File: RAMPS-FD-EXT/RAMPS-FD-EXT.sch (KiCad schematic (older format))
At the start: 23 parts, among them J101 NET-TIE, M101 LOGO_OSHW, M102 PCB_GREEN_RMC, P101 CONN_2, P102 CONN_2, P103 CONN_10, U101 LM7809, U102 74HC595, U103 74HC595

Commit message: EXT4: update schematic, layout
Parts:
- removed P103: CONN_10, symbol CONN_10
- added P103: CONN_4, symbol CONN_4
- added P104: CONN_4X2, symbol CONN_4X2
- gave numbers to parts that had none: 1
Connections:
- net labels added: +5V
- wire segments 75 -> 79
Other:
- moved on the sheet: C101, C104, F101, F102, H101, H102, H103, H104, J101, J102, M101, M102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

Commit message: RAMPS-FD-EXT: update, schematic, routing and gerbers
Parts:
- added JP101: VLOG_SEL, ~, symbol JUMP_MINI_3
- P101: value CONN_2 -> MOTOR
- P102: value CONN_2 -> HEATER
- P103: value CONN_4 -> I2C
- P104: value CONN_4X2 -> SPI
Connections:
- net +5V: now also JP101.3
- net +V_LOGIC: now also JP101.2; no longer P103.1 (P1)
- new net VREF: JP101.1, P103.1 (P1)
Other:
- note added: "Select logic voltage"
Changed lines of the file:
@@
 Sheet 1 4
 Title ""
-Date "26 sep 2013"
+Date "6 oct 2013"
 Rev ""
 Comp ""
@@
 L VCC #PWR02
 U 1 1 523CE64B
-P 1850 2400
-F 0 "#PWR02" H 1850 2500 30  0001 C CNN
-F 1 "VCC" H 1850 2500 30  0000 C CNN
-F 2 "" H 1850 2400 60  0001 C CNN
-F 3 "" H 1850 2400 60  0001 C CNN
-	1    1850 2400
+P 3400 3650
+F 0 "#PWR02" H 3400 3750 30  0001 C CNN
+F 1 "VCC" H 3400 3750 30  0000 C CNN
+F 2 "" H 3400 3650 60  0001 C CNN
+F 3 "" H 3400 3650 60  0001 C CNN
+	1    3400 3650
 	1    0    0    -1
 $EndComp
@@
 $Comp
 L PWR_FLAG #FLG014
-U 1 1 523B8CDB
-P 2200 2450
-F 0 "#FLG014" H 2200 2545 30  0001 C CNN
-F 1 "PWR_FLAG" H 2200 2630 30  0000 C CNN
-F 2 "" H 2200 2450 60  0001 C CNN
-F 3 "" H 2200 2450 60  0001 C CNN
-	1    2200 2450
-	1    0    0    -1
-$EndComp
-$Comp
-L PWR_FLAG #FLG015
 U 1 1 523B8CDA
 P 3150 5350
-F 0 "#FLG015" H 3150 5445 30  0001 C CNN
+F 0 "#FLG014" H 3150 5445 30  0001 C CNN
 F 1 "PWR_FLAG" H 3150 5530 30  0000 C CNN
 F 2 "" H 3150 5350 60  0001 C CNN
@@
 $EndComp
 $Comp
-L PWR_FLAG #FLG016
+L PWR_FLAG #FLG015
 U 1 1 523B8CD9
 P 2700 4400
-F 0 "#FLG016" H 2700 4495 30  0001 C CNN
+F 0 "#FLG015" H 2700 4495 30  0001 C CNN
 F 1 "PWR_FLAG" H 2700 4580 30  0000 C CNN
 F 2 "" H 2700 4400 60  0001 C CNN
@@
 $EndSheet
 $Comp
-L GNDPWR #PWR017
+L GNDPWR #PWR016
 U 1 1 523B79D2
 P 2700 5700
-F 0 "#PWR017" H 2700 5750 40  0001 C CNN
+F 0 "#PWR016" H 2700 5750 40  0001 C CNN
 F 1 "GNDPWR" H 2700 5620 40  0000 C CNN
 F 2 "" H 2700 5700 60  0001 C CNN
@@
 $EndComp
 $Comp
-L GNDPWR #PWR018
+L GNDPWR #PWR017
 U 1 1 523B79C1
 P 2400 4650
-F 0 "#PWR018" H 2400 4700 40  0001 C CNN
+F 0 "#PWR017" H 2400 4700 40  0001 C CNN
 F 1 "GNDPWR" H 2400 4570 40  0000 C CNN
 F 2 "" H 2400 4650 60  0001 C CNN
@@
 $EndComp
 $Comp
-L GND #PWR019
+L GND #PWR018
 U 1 1 523B79A8
 P 1450 1600
-F 0 "#PWR019" H 1450 1600 30  0001 C CNN
+F 0 "#PWR018" H 1450 1600 30  0001 C CNN
 F 1 "GND" H 1450 1530 30  0001 C CNN
 F 2 "" H 1450 1600 60  0001 C CNN
@@
 $EndComp
 $Comp
-L +V_LOGIC #PWR020
+L +V_LOGIC #PWR019
 U 1 1 523B7997
-P 1550 2400
-F 0 "#PWR020" H 1550 2370 30  0001 C CNN
-F 1 "+V_LOGIC" H 1550 2500 30  0000 C CNN
-F 2 "" H 1550 2400 60  0001 C CNN
-F 3 "" H 1550 2400 60  0001 C CNN
-	1    1550 2400
-	1    0    0    -1
-$EndComp
-$Comp
-L +V_POWER #PWR021
+P 3100 3650
+F 0 "#PWR019" H 3100 3620 30  0001 C CNN
+F 1 "+V_LOGIC" H 3100 3750 30  0000 C CNN
+F 2 "" H 3100 3650 60  0001 C CNN
+F 3 "" H 3100 3650 60  0001 C CNN
+	1    3100 3650
+	1    0    0    -1
+$EndComp
+$Comp
+L +V_POWER #PWR020
 U 1 1 523B798A
 P 2700 5350
-F 0 "#PWR021" H 2700 5320 30  0001 C CNN
+F 0 "#PWR020" H 2700 5320 30  0001 C CNN
 F 1 "+V_POWER" H 2700 5450 30  0000 C CNN
 F 2 "" H 2700 5350 60  0001 C CNN
@@
 $EndComp
 $Comp
-L +V_MOTOR #PWR022
+L +V_MOTOR #PWR021
 U 1 1 523B7983
 P 2400 4350
-F 0 "#PWR022" H 2400 4320 30  0001 C CNN
+F 0 "#PWR021" H 2400 4320 30  0001 C CNN
 F 1 "+V_MOTOR" H 2400 4450 30  0000 C CNN
 F 2 "" H 2400 4350 60  0001 C CNN
@@
 P 1250 5500
 F 0 "P102" V 1200 5500 40  0000 C CNN
-F 1 "CONN_2" V 1300 5500 40  0000 C CNN
+F 1 "HEATER" V 1300 5500 40  0000 C CNN
 F 2 "" H 1250 5500 60  0001 C CNN
 F 3 "" H 1250 5500 60  0001 C CNN
@@
 P 1250 4500
 F 0 "P101" V 1200 4500 40  0000 C CNN
-F 1 "CONN_2" V 1300 4500 40  0000 C CNN
+F 1 "MOTOR" V 1300 4500 40  0000 C CNN
 F 2 "" H 1250 4500 60  0001 C CNN
 F 3 "" H 1250 4500 60  0001 C CNN
@@
 	2400 4350 2400 4400
 Wire Wire Line
-	1550 2400 1550 2450
+	3100 3650 3100 3900
 Wire Wire Line
 	1450 1600 1450 1500
@@
 Wire Wire Line
 	7100 3500 6850 3500
-Wire Wire Line
-	1250 2450 2200 2450
-Connection ~ 1550 2450
 Wire Wire Line
 	3150 5400 3150 5350
@@
 	2000 7000 3300 7000
 Wire Wire Line
-	1850 2400 1850 2450
-Connection ~ 1850 2450
+	3400 3900 3400 3650
 Wire Wire Line
 	3000 2650 3000 2600
@@
 $EndComp
 $Comp
-L GND #PWR023
+L GND #PWR022
 U 1 1 523DE100
 P 4000 5650
-F 0 "#PWR023" H 4000 5650 30  0001 C CNN
+F 0 "#PWR022" H 4000 5650 30  0001 C CNN
 F 1 "GND" H 4000 5580 30  0001 C CNN
 F 2 "" H 4000 5650 60  0001 C CNN
@@
 	1400 6450 1550 6450
 $Comp
-L PWR_FLAG #FLG024
+L PWR_FLAG #FLG023
 U 1 1 52437008
 P 2000 6450
-F 0 "#FLG024" H 2000 6545 30  0001 C CNN
+F 0 "#FLG023" H 2000 6545 30  0001 C CNN
 F 1 "PWR_FLAG" H 2000 6630 30  0000 C CNN
 F 2 "" H 2000 6450 60  0001 C CNN
@@
 P 900 2600
 F 0 "P103" V 850 2600 50  0000 C CNN
-F 1 "CONN_4" V 950 2600 50  0000 C CNN
+F 1 "I2C" V 950 2600 50  0000 C CNN
 F 2 "" H 900 2600 60  0000 C CNN
 F 3 "" H 900 2600 60  0000 C CNN
@@
 $EndComp
 $Comp
-L GND #PWR025
+L GND #PWR024
 U 1 1 52448887
 P 1550 2950
-F 0 "#PWR025" H 1550 2950 30  0001 C CNN
+F 0 "#PWR024" H 1550 2950 30  0001 C CNN
 F 1 "GND" H 1550 2880 30  0001 C CNN
 F 2 "" H 1550 2950 60  0001 C CNN
@@
 P 1950 1350
 F 0 "P104" H 1950 1600 50  0000 C CNN
-F 1 "CONN_4X2" V 1950 1350 40  0000 C CNN
+F 1 "SPI" V 1950 1350 40  0000 C CNN
 F 2 "" H 1950 1350 60  0000 C CNN
 F 3 "" H 1950 1350 60  0000 C CNN
@@
 $EndComp
 $Comp
-L +5V #PWR026
+L +5V #PWR025
 U 1 1 52448919
 P 1300 1100
-F 0 "#PWR026" H 1300 1190 20  0001 C CNN
+F 0 "#PWR025" H 1300 1190 20  0001 C CNN
 F 1 "+5V" H 1300 1190 30  0000 C CNN
 F 2 "" H 1300 1100 60  0000 C CNN
@@
 	1550 1300 1050 1300
 $Comp
-L PWR_FLAG #FLG027
+L PWR_FLAG #FLG026
 U 1 1 52448EF8
 P 850 1200
-F 0 "#FLG027" H 850 1295 30  0001 C CNN
+F 0 "#FLG026" H 850 1295 30  0001 C CNN
 F 1 "PWR_FLAG" H 850 1380 30  0000 C CNN
 F 2 "" H 850 1200 60  0001 C CNN
@@
 $EndComp
 Connection ~ 1300 1200
+$Comp
+L JUMP_MINI_3 JP101
+U 1 1 5251B1D4
+P 2500 3550
+F 0 "JP101" H 2500 3725 60  0000 C CNN
+F 1 "VLOG_SEL" H 2525 3375 60  0000 C CNN
+F 2 "~" H 2500 3550 60  0000 C CNN
+F 3 "~" H 2500 3550 60  0000 C CNN
+	1    2500 3550
+	1    0    0    -1
+$EndComp
+Wire Wire Line
+	2500 3650 2500 3900
+Wire Wire Line
+	2500 3900 3600 3900
+Connection ~ 3100 3900
+$Comp
+L PWR_FLAG #FLG027
+U 1 1 5251B30C
+P 3600 3900
+F 0 "#FLG027" H 3600 3995 30  0001 C CNN
+F 1 "PWR_FLAG" H 3600 4080 30  0000 C CNN
+F 2 "" H 3600 3900 60  0001 C CNN
+F 3 "" H 3600 3900 60  0001 C CNN
+	1    3600 3900
+	1    0    0    -1
+$EndComp
+Connection ~ 3400 3900
+Text GLabel 1650 2450 2    50   Output ~ 0
+VREF
+Wire Wire Line
+	1650 2450 1250 2450
+Text GLabel 1850 3550 0    50   Input ~ 0
+VREF
+Wire Wire Line
+	1850 3550 2350 3550
+$Comp
+L +5V #PWR028
+U 1 1 5251B4FF
+P 2800 3450
+F 0 "#PWR028" H 2800 3540 20  0001 C CNN
+F 1 "+5V" H 2800 3540 30  0000 C CNN
+F 2 "" H 2800 3450 60  0000 C CNN
+F 3 "" H 2800 3450 60  0000 C CNN
+	1    2800 3450
+	1    0    0    -1
+$EndComp
+Wire Wire Line
+	2800 3450 2800 3550
+Wire Wire Line
+	2800 3550 2650 3550
+Text Notes 2200 3250 0    50   ~ 0
+Select logic voltage
 $EndSCHEMATC

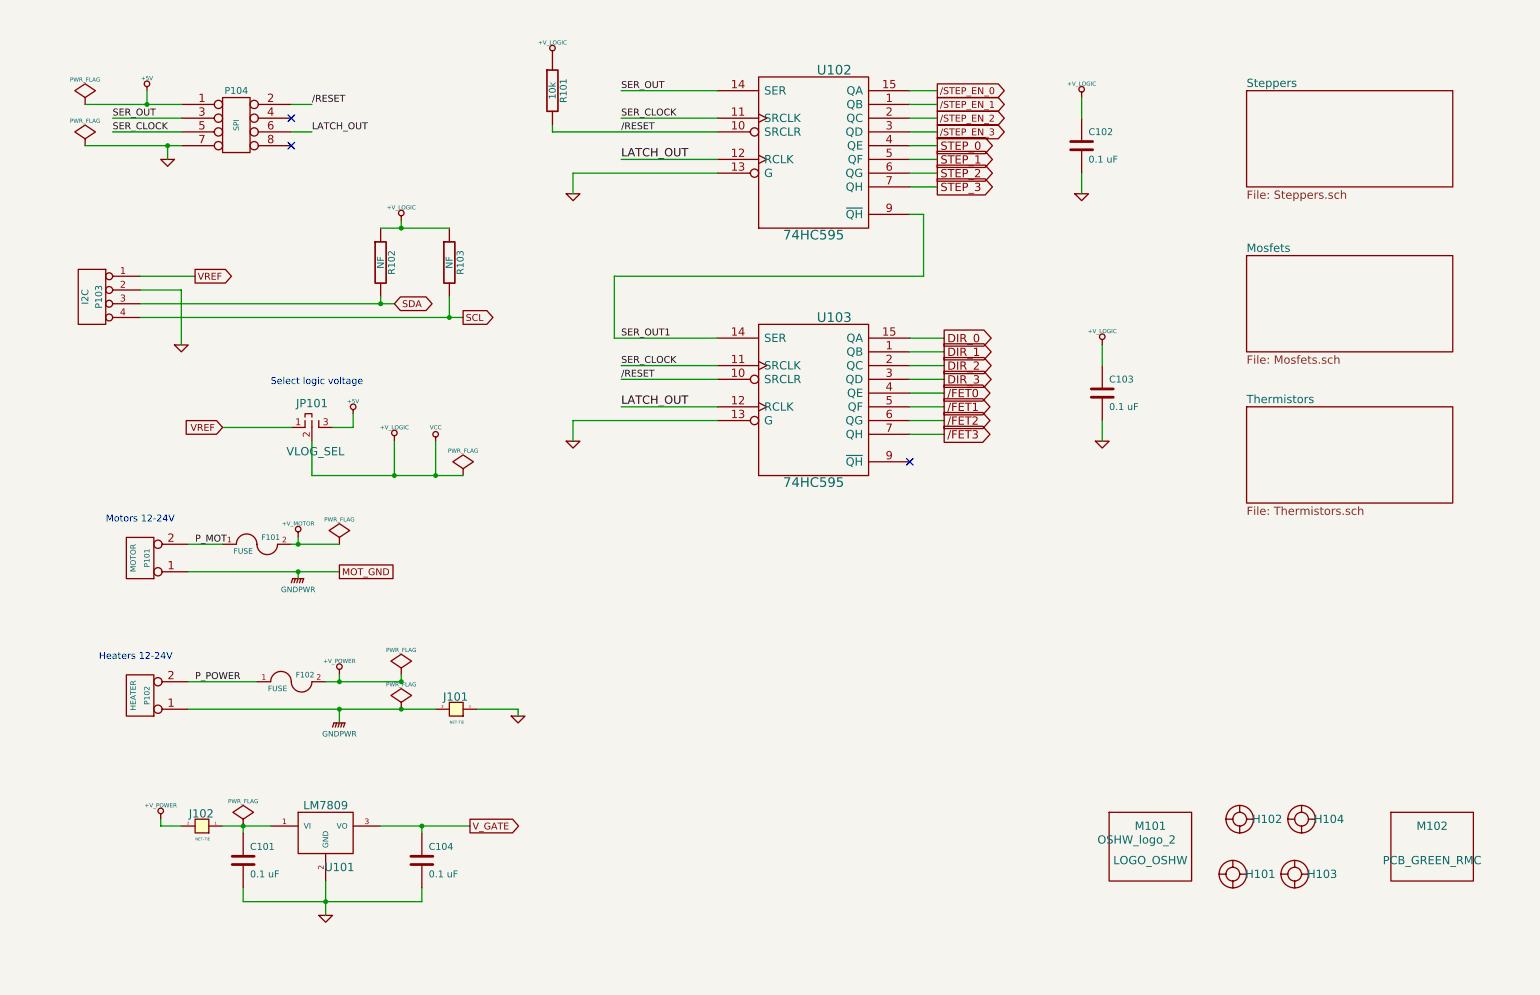
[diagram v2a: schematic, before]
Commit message: RAMPS-FD: new version with 6 extruders
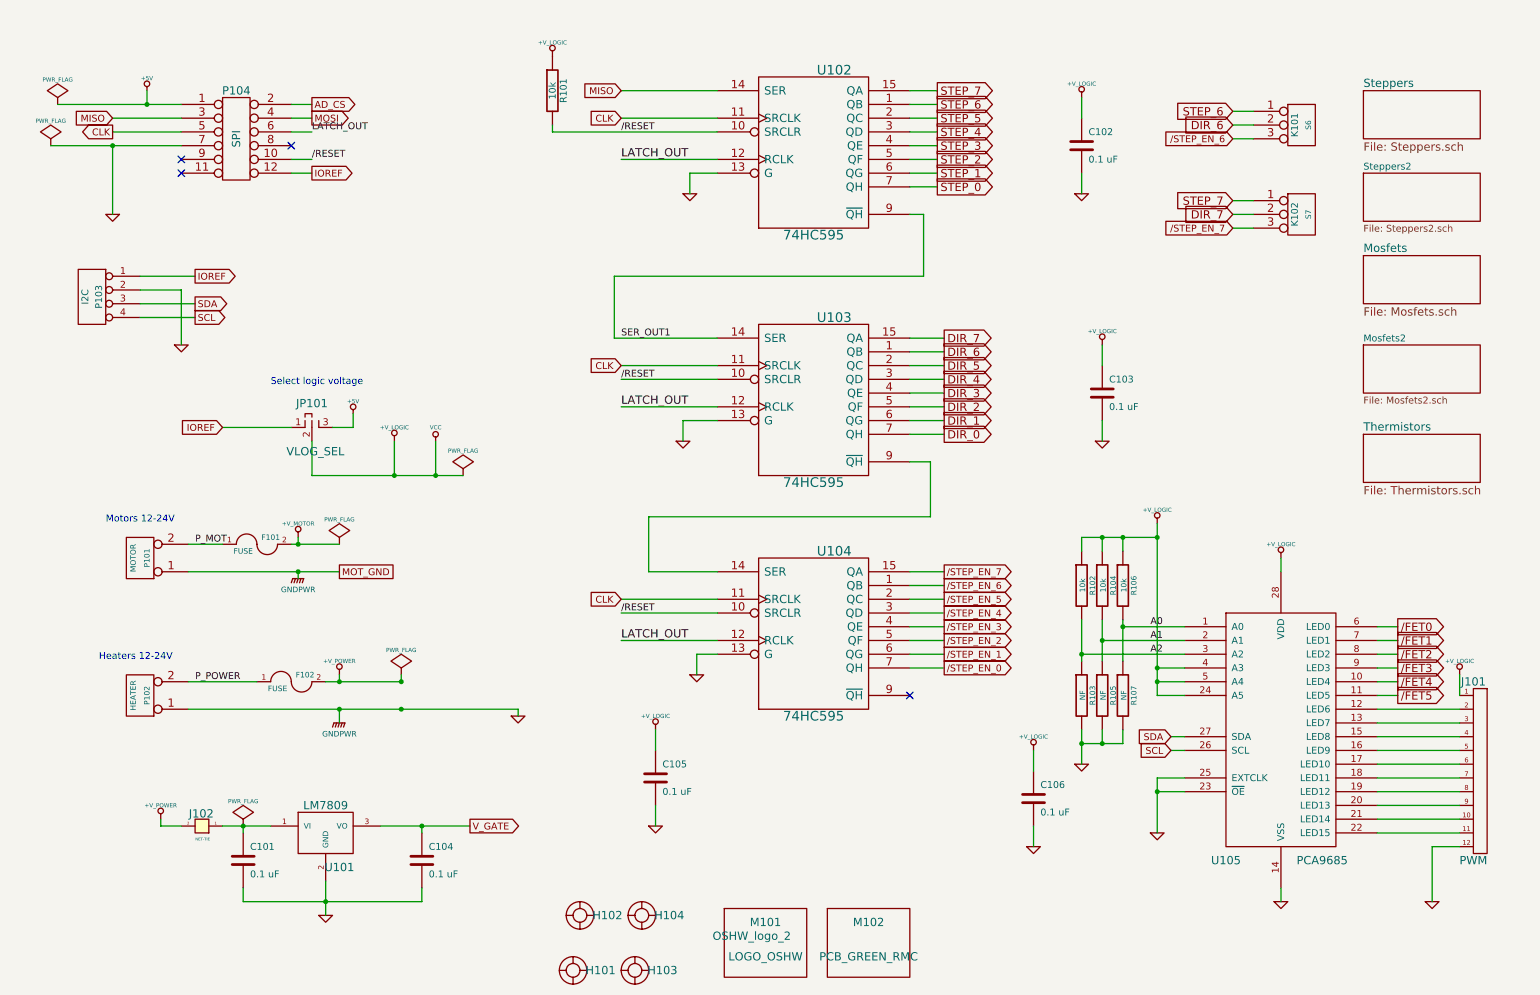
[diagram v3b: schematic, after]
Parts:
- removed J101: NET-TIE, TIE-1MM, symbol NET-TIE
- removed P104: SPI, symbol CONN_4X2
- added C105, C106: 0.1 uF, symbol C
- added J101: PWM, symbol HEADER_12
- added K101: S6, symbol CONN_3
- added K102: S7, symbol CONN_3
- added P104: SPI, symbol CONN_6X2
- added R104, R106: 10k, ~, symbol R
- added R105, R107: NF, ~, symbol R
- added U104: 74HC595, symbol 74HC595
- added U105: PCA9685, symbol PCA9685
- R102: value NF -> 10k; footprint (none) -> ~
- R103: footprint (none) -> ~
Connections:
- net GNDPWR is gone; now on net GND: P101.1 (P1), P102.1 (P1)
- net +5V: now also P104.1 (P1)
- net +V_LOGIC: now also C105.1, C106.1, J101.1, R104.1, R106.1, U104.16 (VCC), U105.24 (A5), U105.28 (VDD), U105.4 (A3), U105.5 (A4); no longer R103.1
- net /FET0: now also U105.6 (LED0); no longer U103.4 (QE)
- net /FET1: now also U105.7 (LED1); no longer U103.5 (QF)
- net /FET2: now also U105.8 (LED2); no longer U103.6 (QG)
- net /FET3: now also U105.9 (LED3); no longer U103.7 (QH)
- net /RESET: now also P104.10, U104.10 (SRCLR)
- net /STEP_EN_0: now also U104.7 (QH); no longer U102.15 (QA)
- net /STEP_EN_1: now also U104.6 (QG); no longer U102.1 (QB)
- net /STEP_EN_2: now also U104.5 (QF); no longer U102.2 (QC)
- net /STEP_EN_3: now also U104.4 (QE); no longer U102.3 (QD)
- net DIR_0: now also U103.7 (QH); no longer U103.15 (QA)
- net DIR_1: now also U103.6 (QG); no longer U103.1 (QB)
- net DIR_2: now also U103.5 (QF); no longer U103.2 (QC)
- net DIR_3: now also U103.4 (QE); no longer U103.3 (QD)
- net GND: now also R103.2, C105.2, C106.2, J101.12, P104.7 (P7), R105.2, R107.2, U104.13 (G), U104.8 (GND), U105.14 (VSS), U105.23 (~OE), U105.25 (EXTCLK)
- net LATCH_OUT: now also P104.6 (P6), U104.12 (RCLK)
- net SCL: now also U105.26 (SCL); no longer R103.2
- net SDA: now also U105.27 (SDA); no longer R102.2
- net STEP_0: now also U102.7 (QH); no longer U102.4 (QE)
- net STEP_1: now also U102.6 (QG); no longer U102.5 (QF)
- net STEP_2: now also U102.5 (QF); no longer U102.6 (QG)
- net STEP_3: now also U102.4 (QE); no longer U102.7 (QH)
- net at U103.9 (~QH): now also U104.14 (SER)
- net SER_CLOCK renamed CLK
- net CLK: now also P104.5 (P5), U104.11 (SRCLK)
- net SER_OUT renamed MISO
- net MISO: now also P104.3 (P3)
- net VREF renamed IOREF
- net IOREF: now also P104.12
- new net: J101.2, U105.12 (LED6)
- new net: J101.3, U105.13 (LED7)
- new net: J101.4, U105.15 (LED8)
- new net: J101.5, U105.16 (LED9)
- new net: J101.6, U105.17 (LED10)
- new net: J101.7, U105.18 (LED11)
- new net: J101.8, U105.19 (LED12)
- new net: J101.9, U105.20 (LED13)
- new net: J101.10, U105.21 (LED14)
- new net: J101.11, U105.22 (LED15)
- new net /FET4: U105.10 (LED4)
- new net /FET5: U105.11 (LED5)
- new net /STEP_EN_4: U104.3 (QD)
- new net /STEP_EN_5: U104.2 (QC)
- new net /STEP_EN_6: K101.3 (P3), U104.1 (QB)
- new net /STEP_EN_7: K102.3 (P3), U104.15 (QA)
- new net A0: R106.2, R107.1, U105.1 (A0)
- new net A1: R104.2, R105.1, U105.2 (A1)
- new net A2: R102.2, R103.1, U105.3 (A2)
- new net AD_CS: P104.2 (P2)
- new net DIR_4: U103.3 (QD)
- new net DIR_5: U103.2 (QC)
- new net DIR_6: K101.2 (PM), U103.1 (QB)
- new net DIR_7: K102.2 (PM), U103.15 (QA)
- new net MOSI: P104.4 (P4)
- new net STEP_4: U102.3 (QD)
- new net STEP_5: U102.2 (QC)
- new net STEP_6: K101.1 (P1), U102.1 (QB)
- new net STEP_7: K102.1 (P1), U102.15 (QA)
- no-connect marks 3 -> 4
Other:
- moved on the sheet: H101, H102, H103, H104, M101, M102
